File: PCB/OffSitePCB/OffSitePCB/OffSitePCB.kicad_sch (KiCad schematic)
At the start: 0 parts

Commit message: added 2 parts on kicad library asteria Nova
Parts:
- added U1: ~, symbol ASTERIA_NOVA_LIB:MaixCam
- added U2: ~, symbol ASTERIA_NOVA_LIB:E220-900T22D
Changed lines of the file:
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@@
 	(generator_version "9.0")
 	(paper "A4")
+	(symbol
+		(lib_id "ASTERIA_NOVA_LIB:MaixCam")
+		(at 92.71 62.23 0)
+		(unit 1)
+		(exclude_from_sim no)
+		(in_bom yes)
+		(on_board yes)
+		(dnp no)
+		(fields_autoplaced yes)
+		(property "Reference" "U1"
+			(at 108.8233 105.41 0)
+			(effects
+				(font
+					(size 1.27 1.27)
+				)
+				(justify left)
+			)
+		)
+		(property "Value" "~"
+			(at 108.8233 106.68 0)
+			(effects
+				(font
+					(size 1.27 1.27)
+				)
+				(justify left)
+			)
+		)
+		(property "Footprint" ""
+			(at 92.71 62.23 0)
+			(effects
+				(font
+					(size 1.27 1.27)
+				)
+				(hide yes)
+			)
+		)
+		(property "Datasheet" ""
+			(at 92.71 62.23 0)
+			(effects
+				(font
+					(size 1.27 1.27)
+				)
+				(hide yes)
+			)
+		)
+		(property "Description" ""
+			(at 92.71 62.23 0)
+			(effects
+				(font
+					(size 1.27 1.27)
+				)
+				(hide yes)
+			)
+		)
+		(pin ""
+		)
+		(pin ""
+		)
+		(pin ""
+		)
+		(pin ""
+		)
+		(pin ""
+		)
+		(pin ""
+		)
+		(pin ""
+		)
+		(pin ""
+		)
+		(pin ""
+		)
+		(pin ""
+		)
+		(pin ""
+		)
+		(pin ""
+		)
+		(pin ""
+		)
+		(pin ""
+		)
+		(pin ""
+		)
+		(pin ""
+		)
+		(pin ""
+		)
+		(pin ""
+		)
+		(pin ""
+		)
+		(pin ""
+		)
+		(pin ""
+		)
+		(pin ""
+		)
+		(pin ""
+		)
+		(pin ""
+		)
+		(pin ""
+		)
+		(pin ""
+		)
+		(pin ""
+		)
+		(pin ""
+		)
+		(pin ""
+		)
+		(instances
+			(project ""
+				(path "/6f66eba4-6760-490a-ac08-5b04c32a5ed7"
+					(reference "U1")
+					(unit 1)
+				)
+			)
+		)
+	)
+	(symbol
+		(lib_id "ASTERIA_NOVA_LIB:E220-900T22D")
+		(at 154.94 64.77 0)
+		(unit 1)
+		(exclude_from_sim no)
+		(in_bom yes)
+		(on_board yes)
+		(dnp no)
+		(fields_autoplaced yes)
+		(property "Reference" "U2"
+			(at 163.4333 60.96 0)
+			(effects
+				(font
+					(size 1.27 1.27)
+				)
+				(justify left)
+			)
+		)
+		(property "Value" "~"
+			(at 163.4333 63.5 0)
+			(effects
+				(font
+					(size 1.27 1.27)
+				)
+				(justify left)
+			)
+		)
+		(property "Footprint" ""
+			(at 154.94 64.77 0)
+			(effects
+				(font
+					(size 1.27 1.27)
+				)
+				(hide yes)
+			)
+		)
+		(property "Datasheet" ""
+			(at 154.94 64.77 0)
+			(effects
+				(font
+					(size 1.27 1.27)
+				)
+				(hide yes)
+			)
+		)
+		(property "Description" ""
+			(at 154.94 64.77 0)
+			(effects
+				(font
+					(size 1.27 1.27)
+				)
+				(hide yes)
+			)
+		)
+		(pin ""
+		)
+		(pin ""
+		)
+		(pin ""
+		)
+		(pin ""
+		)
+		(pin ""
+		)
+		(pin ""
+		)
+		(pin ""
+		)
+		(instances
+			(project ""
+				(path "/6f66eba4-6760-490a-ac08-5b04c32a5ed7"
+					(reference "U2")
+					(unit 1)
+				)
+			)
+		)
+	)
 	(sheet_instances
 		(path "/"

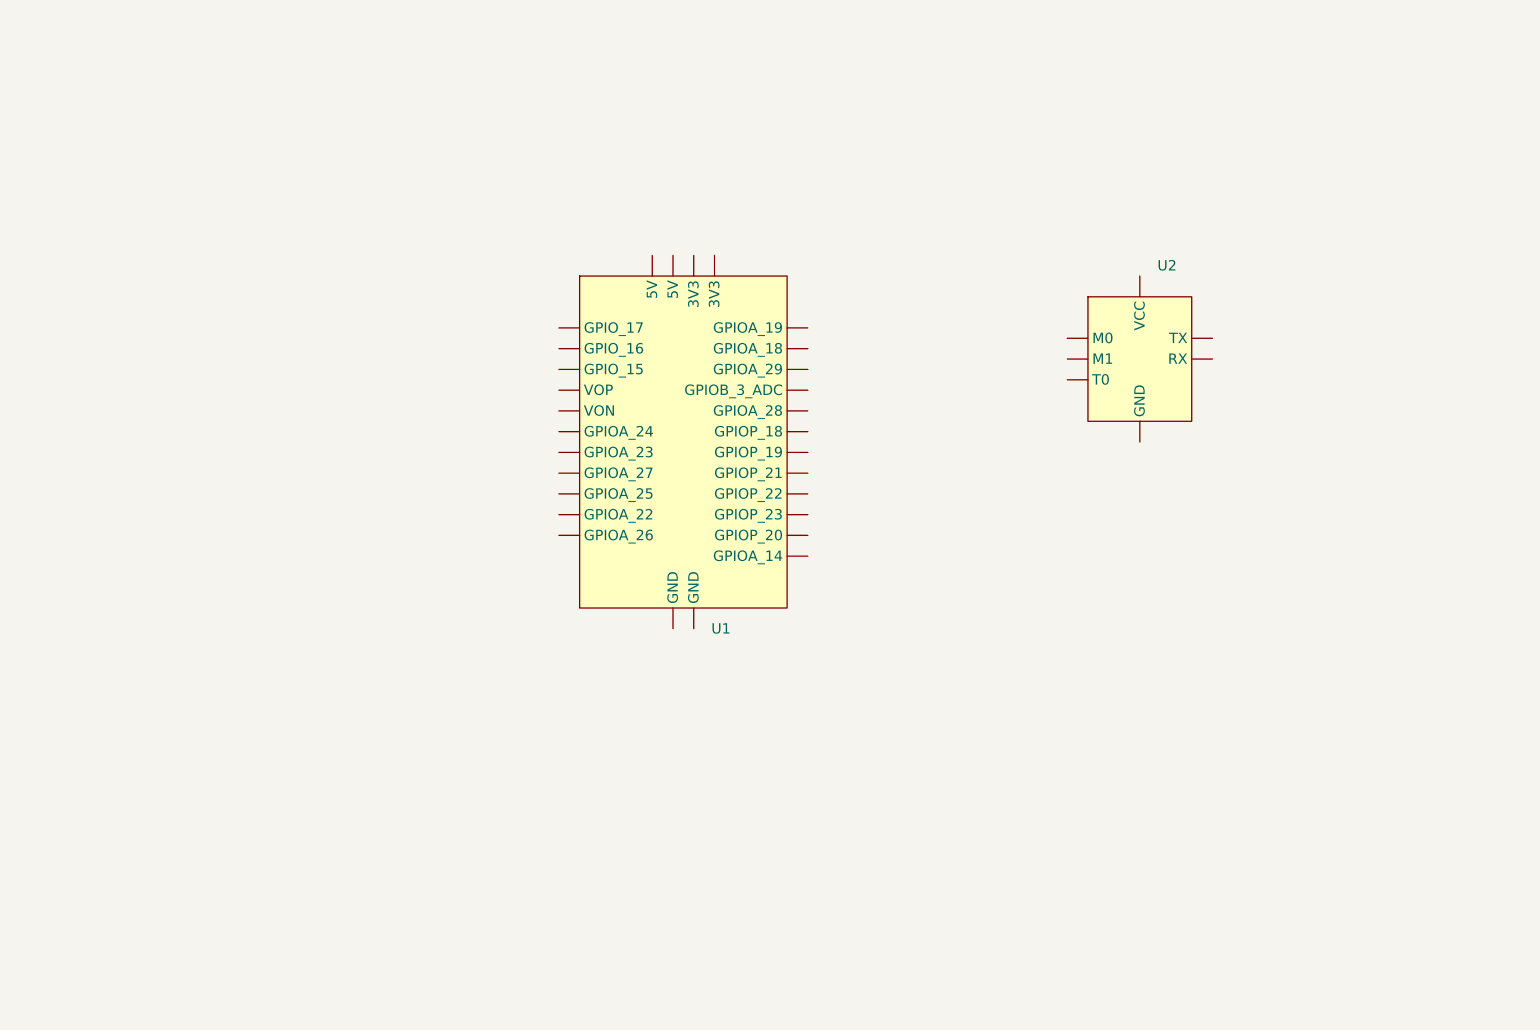
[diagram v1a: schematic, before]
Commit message: usb-c power input
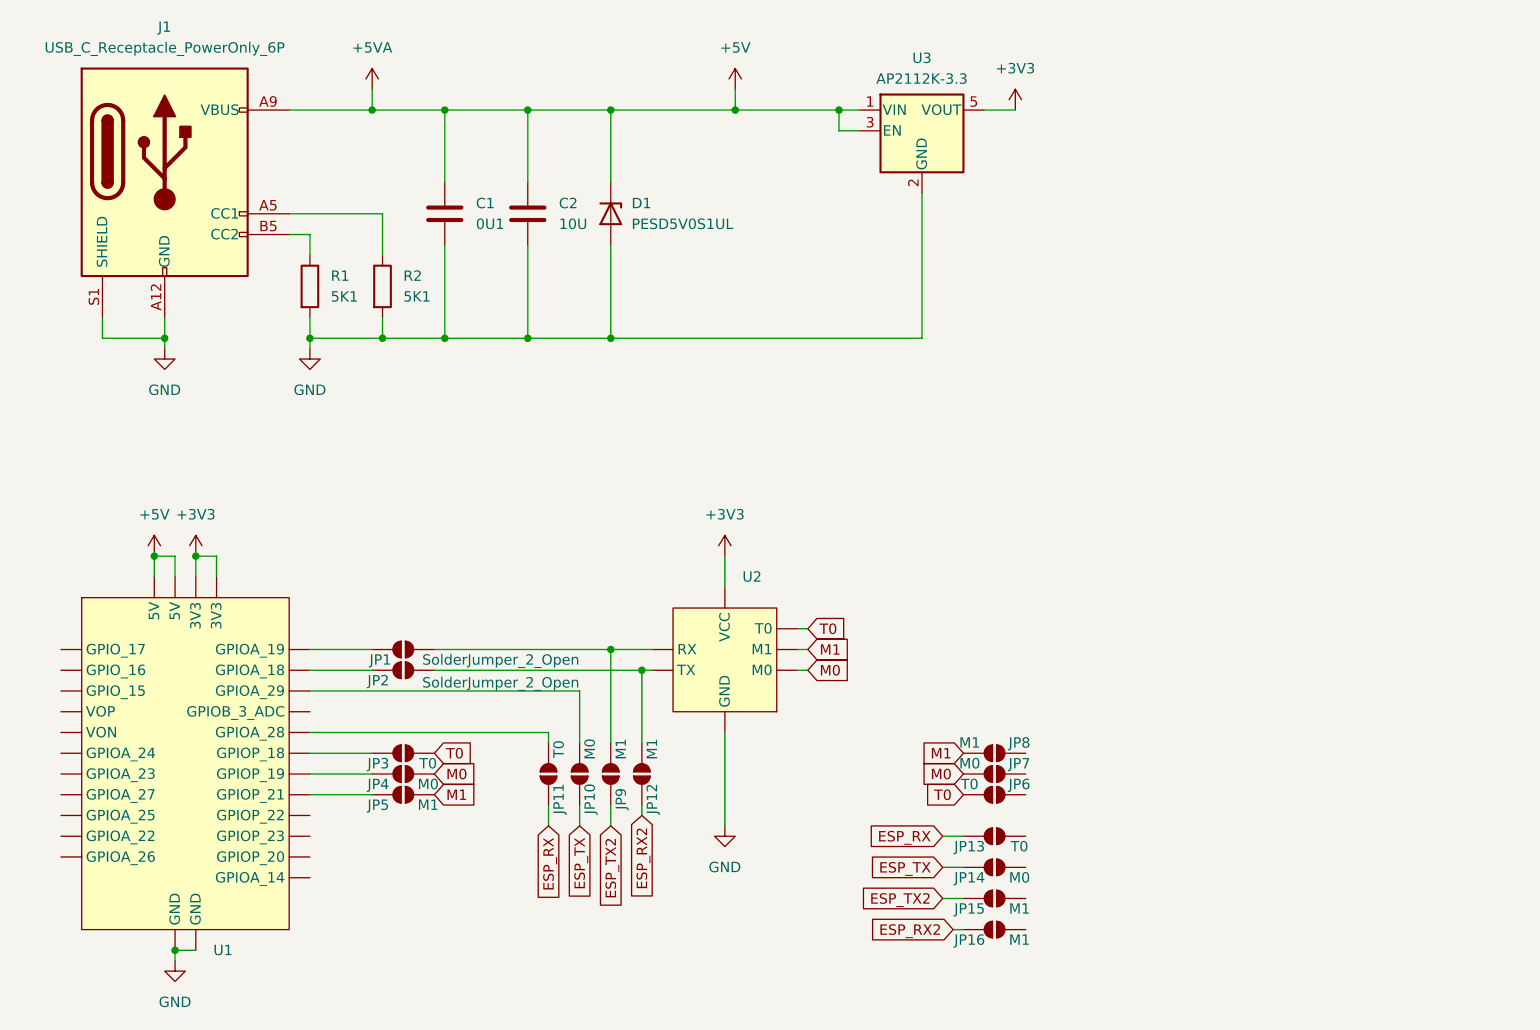
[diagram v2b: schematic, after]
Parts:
- added C1: 0U1, symbol Device:C
- added C2: 10U, symbol Device:C
- added D1: PESD5V0S1UL, Diode_SMD:D_SOD-882, symbol Diode:PESD5V0S1UL
- added J1: USB_C_Receptacle_PowerOnly_6P, symbol Connector:USB_C_Receptacle_PowerOnly_6P
- added JP1, JP2: SolderJumper_2_Open, symbol Jumper:SolderJumper_2_Open
- added JP10, JP14, JP4, JP7: M0, symbol Jumper:SolderJumper_2_Open
- added JP11, JP13, JP3, JP6: T0, symbol Jumper:SolderJumper_2_Open
- added JP12, JP15, JP16, JP5, JP8, JP9: M1, symbol Jumper:SolderJumper_2_Open
- added R1, R2: 5K1, symbol Device:R
- added U3: AP2112K-3.3, Package_TO_SOT_SMD:SOT-23-5, symbol Regulator_Linear:AP2112K-3.3
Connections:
- net GND: now reaches U1. (GPIOA_14)
- net GND: now also U2. (RX), C1.2, C2.2, D1.2 (A), J1.A12 (GND), J1.B12 (GND), J1.S1 (SHIELD), R1.2, R2.2, U3.2 (GND)
- net T0: now reaches U2. (RX)
- net T0: now also JP3.2 (B), JP6.2 (B)
- new net: JP12.2 (B), JP2.2 (B), U2. (RX)
- new net: JP1.2 (B), JP9.2 (B), U2. (RX)
- new net: JP2.1 (A), U1. (GPIOA_14)
- new net: J1.A5 (CC1), R2.1
- new net: J1.B5 (CC2), R1.1
- new net: JP10.2 (B), U1. (GPIOA_14)
- new net: JP3.1 (A), U1. (GPIOA_14)
- new net: JP4.1 (A), U1. (GPIOA_14)
- new net: JP11.2 (B), U1. (GPIOA_14)
- new net: JP5.1 (A), U1. (GPIOA_14)
- new net: JP1.1 (A), U1. (GPIOA_14)
- new net +3V3: U1. (GPIOA_14), U2. (RX), U3.5 (VOUT)
- new net +5V: C1.1, C2.1, D1.1 (K), J1.A9 (VBUS), J1.B9 (VBUS), U1. (GPIOA_14), U3.1 (VIN), U3.3 (EN)
- new net ESP_RX: JP11.1 (A), JP13.1 (A)
- new net ESP_RX2: JP12.1 (A), JP16.1 (A)
- new net ESP_TX: JP10.1 (A), JP14.1 (A)
- new net ESP_TX2: JP15.1 (A), JP9.1 (A)
- new net M0: JP4.2 (B), JP7.2 (B), U2. (RX)
- new net M1: JP5.2 (B), JP8.2 (B), U2. (RX)
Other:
- moved on the sheet: U1

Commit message: added datasheet for Buck , As well as LicheeRV nano for future use and reference
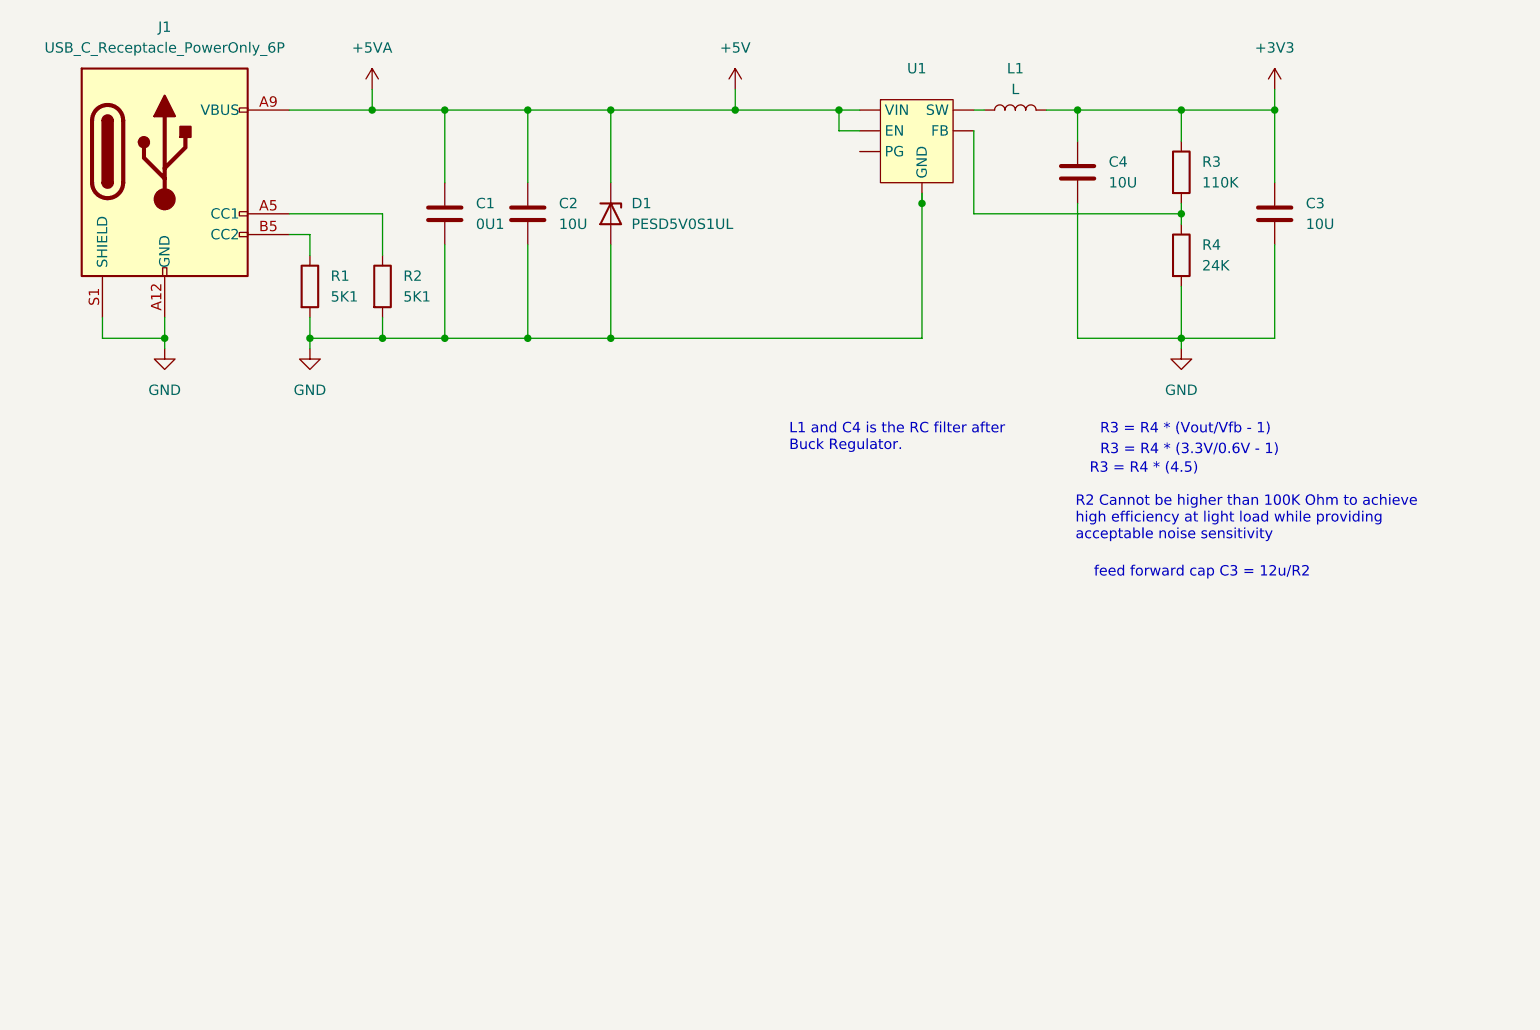
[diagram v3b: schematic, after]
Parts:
- removed JP1, JP2: SolderJumper_2_Open, symbol Jumper:SolderJumper_2_Open
- removed JP10, JP14, JP4, JP7: M0, symbol Jumper:SolderJumper_2_Open
- removed JP11, JP13, JP3, JP6: T0, symbol Jumper:SolderJumper_2_Open
- removed JP12, JP15, JP16, JP5, JP8, JP9: M1, symbol Jumper:SolderJumper_2_Open
- removed U1: ~, symbol ASTERIA_NOVA_LIB:MaixCam
- removed U2: ~, symbol ASTERIA_NOVA_LIB:E220-900T22D
- removed U3: AP2112K-3.3, Package_TO_SOT_SMD:SOT-23-5, symbol Regulator_Linear:AP2112K-3.3
- added C3, C4: 10U, symbol Device:C
- added L1: L, symbol Device:L
- added R3: 110K, symbol Device:R
- added R4: 24K, symbol Device:R
- added U1: ~, symbol ASTERIA_NOVA_LIB:TI_TPS62826
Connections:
- net +3V3: now also C3.1, C4.1, L1.2, R3.1
- net +5V: now also U1. (FB)
- net GND: now also C3.2, C4.2, R4.2, U1. (FB)
- new net: R3.2, R4.1, U1. (FB)
- new net: L1.1, U1. (FB)
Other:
- note added: "L1 and C4 is the RC filter after Buck Regulator."
- note added: "R2 Cannot be higher than 100K Ohm to achieve high efficiency at light load while providing acceptable noise sensitivity"
- note added: "R3 = R4 * (3.3V/0.6V - 1)"
- note added: "R3 = R4 * (4.5)"
- note added: "R3 = R4 * (Vout/Vfb - 1)"
- note added: "feed forward cap C3 = 12u/R2"

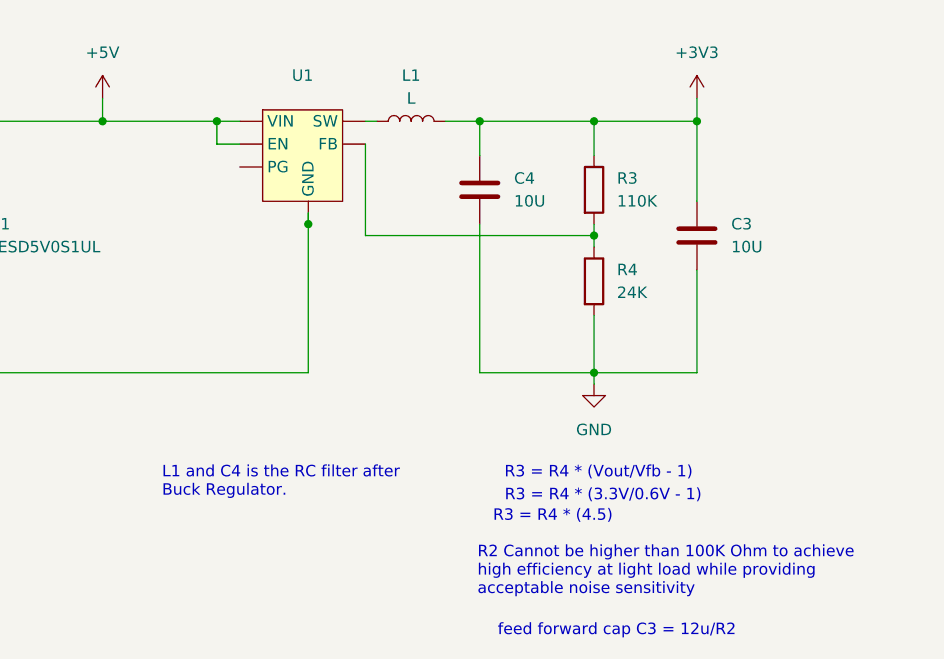
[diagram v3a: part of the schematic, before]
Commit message: RC filter values and Output Cap added
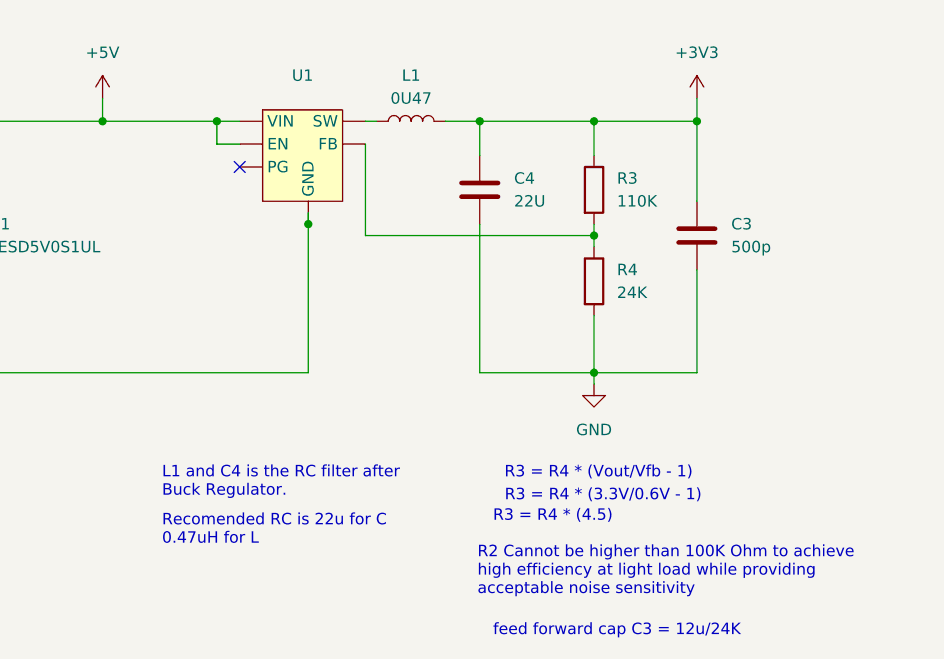
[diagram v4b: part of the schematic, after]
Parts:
- C3: value 10U -> 500p
- C4: value 10U -> 22U
- L1: value L -> 0U47
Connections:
- no-connect marks 0 -> 1
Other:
- note added: "Recomended RC is 22u for C 0.47uH for L"
- note added: "feed forward cap C3 = 12u/24K"
- note removed: "feed forward cap C3 = 12u/R2"
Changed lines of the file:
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@@
+		)
+	)
+	(text "Recomended RC is 22u for C\n0.47uH for L\n"
+		(exclude_from_sim no)
+		(at 118.364 87.376 0)
+		(effects
+			(font
+				(size 1.27 1.27)
+			)
+			(justify left)
 		)
 	)
@@
 		)
 	)
-	(text "feed forward cap C3 = 12u/R2"
+	(text "feed forward cap C3 = 12u/24K"
 		(exclude_from_sim no)
 		(at 168.91 98.552 0)
@@
 		(diameter 0)
 		(color 0 0 0 0)
+	)
+	(no_connect
+		(at 127 46.99)
 	)
 	(wire
@@
 			)
 		)
-		(property "Value" "L"
+		(property "Value" "0U47"
 			(at 146.05 39.37 90)
 			(effects
@@
 			)
 		)
-		(property "Value" "10U"
+		(property "Value" "22U"
 			(at 157.48 50.7999 0)
 			(effects
@@
 			)
 		)
-		(property "Value" "10U"
+		(property "Value" "500p"
 			(at 181.61 55.8799 0)
 			(effects
